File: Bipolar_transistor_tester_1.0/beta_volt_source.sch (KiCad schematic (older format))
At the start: 11 parts, among them IC1 OPA454, Q2 PVG612, U5 CPC1977, U6 CPC1977, U7 CPC1977

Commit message: tester up
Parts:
- added C24, C25: 100n, Capacitor_SMD:C_0805_2012Metric, symbol Device:C
- added R? (x4): 1k 1%, Resistor_SMD:R_0805_2012Metric, symbol Device:R
- U31: renamed from U5; footprint (none) -> OptoDevice:i4-PAC
- U33: renamed from U6; footprint (none) -> OptoDevice:i4-PAC
- U34: renamed from U7; footprint (none) -> OptoDevice:i4-PAC
- renumbered D10 to D7, IC1 to IC3, R14 to R43, R15 to R44, R16 to R45, R17 to R46, R18 to R47, Q2 to U32
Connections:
- net +45V: now also C25.1
- net -45V: now also C24.1
- net GND: now also C24.2, C25.2
- net at IC3.6, U32.6: now also U33.2, U34.2; no longer U33.4, U34.4
- net 6_bvs1: now reaches U31.3
- net at U31.4: now also R?.1
- net to_collector: now reaches U34.1
- net to_base: now reaches U33.1
- net at U32.1: now also R?.1
- net 6_bvs2: now reaches U32.2
- net dac renamed dac1
- net feedback renamed collector_feedback
- net out_base renamed 6_bvs4
- net out_collector renamed 6_bvs3
- new net: R?.1, U34.4
- new net: R?.1, U33.4
- new net 6_com_an: R?.2, R?.2, R?.2, R?.2
- no-connect marks 1 -> 3

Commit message: tester up
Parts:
- removed U33: CPC1977, OptoDevice:i4-PAC, symbol Relay_SolidState:CPC1977
- added U33: PVG612, Package_DIP:DIP-6_W7.62mm, symbol Relay_SolidState:PVG612
- gave numbers to parts that had none: 4
- renumbered R43 to R59, R44 to R60, R45 to R62, R46 to R63, R47 to R64
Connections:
- net 6_bvs4: now also U33.2
- net to_base: now also U33.6
- net at IC3.6, U32.6, U34.2: now also U33.4
- net at R66.1: now also U33.1
- no-connect marks 3 -> 4
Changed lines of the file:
@@
 Sheet 8 11
 Title ""
-Date ""
+Date "2022-04-25"
 Rev ""
 Comp ""
@@
 $EndComp
 $Comp
-L Device:R R45
+L Device:R R62
 U 1 1 626C0321
 P 5125 4200
-F 0 "R45" H 5195 4246 50  0000 L CNN
+F 0 "R62" H 5195 4246 50  0000 L CNN
 F 1 "1M 1%" H 5195 4155 50  0000 L CNN
 F 2 "Resistor_SMD:R_0805_2012Metric" V 5055 4200 50  0001 C CNN
@@
 $EndComp
 $Comp
-L Device:R R44
+L Device:R R60
 U 1 1 626C0D69
 P 4850 3900
-F 0 "R44" V 4643 3900 50  0000 C CNN
+F 0 "R60" V 4643 3900 50  0000 C CNN
 F 1 "200k" V 4734 3900 50  0000 C CNN
 F 2 "Resistor_SMD:R_0805_2012Metric" V 4780 3900 50  0001 C CNN
@@
 $EndComp
 $Comp
-L Device:R R43
+L Device:R R59
 U 1 1 626C163D
 P 4850 3500
-F 0 "R43" V 4643 3500 50  0000 C CNN
+F 0 "R59" V 4643 3500 50  0000 C CNN
 F 1 "200k" V 4734 3500 50  0000 C CNN
 F 2 "Resistor_SMD:R_0805_2012Metric" V 4780 3500 50  0001 C CNN
@@
 $EndComp
 $Comp
-L power:GND #PWR087
+L power:GND #PWR0100
 U 1 1 626C292A
 P 5125 4400
-F 0 "#PWR087" H 5125 4150 50  0001 C CNN
+F 0 "#PWR0100" H 5125 4150 50  0001 C CNN
 F 1 "GND" H 5130 4227 50  0000 C CNN
 F 2 "" H 5125 4400 50  0001 C CNN
@@
 Connection ~ 5125 3900
 $Comp
-L power:GND #PWR086
+L power:GND #PWR099
 U 1 1 626C4849
 P 4500 3500
-F 0 "#PWR086" H 4500 3250 50  0001 C CNN
+F 0 "#PWR099" H 4500 3250 50  0001 C CNN
 F 1 "GND" H 4505 3327 50  0000 C CNN
 F 2 "" H 4500 3500 50  0001 C CNN
@@
 	5450 4275 5450 4200
 $Comp
-L power:-45 #PWR089
+L power:-45 #PWR0102
 U 1 1 626B2C4D
 P 5450 4275
-F 0 "#PWR089" H 5590 4325 50  0001 C CNN
+F 0 "#PWR0102" H 5590 4325 50  0001 C CNN
 F 1 "-45" H 5465 4448 50  0000 C CNN
 F 2 "" H 5450 4275 50  0001 C CNN
@@
 $EndComp
 $Comp
-L power:+45 #PWR088
+L power:+45 #PWR0101
 U 1 1 626B5D57
 P 5450 2825
-F 0 "#PWR088" H 5570 2865 50  0001 C CNN
+F 0 "#PWR0101" H 5570 2865 50  0001 C CNN
 F 1 "+45" H 5465 2998 50  0000 C CNN
 F 2 "" H 5450 2825 50  0001 C CNN
@@
 $EndComp
 $Comp
-L Device:R R46
+L Device:R R63
 U 1 1 626C68FB
 P 5550 2400
-F 0 "R46" V 5343 2400 50  0000 C CNN
+F 0 "R63" V 5343 2400 50  0000 C CNN
 F 1 "1M 1%" V 5434 2400 50  0000 C CNN
 F 2 "Resistor_SMD:R_0805_2012Metric" V 5480 2400 50  0001 C CNN
@@
 Wire Wire Line
 	6350 3700 6550 3700
-$Comp
-L Relay_SolidState:CPC1977 U33
-U 1 1 626F7078
-P 7600 5150
-F 0 "U33" V 7646 4970 50  0000 R CNN
-F 1 "CPC1977" V 7555 4970 50  0000 R CNN
-F 2 "OptoDevice:i4-PAC" H 7600 5200 50  0001 C CNN
-F 3 "" H 7600 5200 50  0001 C CNN
-	1    7600 5150
-	0    1    1    0
-$EndComp
 Text HLabel 8050 4850 2    50   Output ~ 0
 to_base
@@
 	5750 4150 5750 4000
 $Comp
-L power:-45 #PWR091
+L power:-45 #PWR0104
 U 1 1 626FD9F5
 P 5750 4150
-F 0 "#PWR091" H 5890 4200 50  0001 C CNN
+F 0 "#PWR0104" H 5890 4200 50  0001 C CNN
 F 1 "-45" H 5765 4323 50  0000 C CNN
 F 2 "" H 5750 4150 50  0001 C CNN
@@
 	5450 2825 5450 3200
 $Comp
-L Device:R R47
+L Device:R R64
 U 1 1 627039AF
 P 5750 2900
-F 0 "R47" H 5820 2946 50  0000 L CNN
+F 0 "R64" H 5820 2946 50  0000 L CNN
 F 1 "100k" H 5820 2855 50  0000 L CNN
 F 2 "Resistor_SMD:R_0805_2012Metric" V 5680 2900 50  0001 C CNN
@@
 $EndComp
 $Comp
-L power:-45 #PWR092
+L power:-45 #PWR0105
 U 1 1 627066A8
 P 6250 3250
-F 0 "#PWR092" H 6390 3300 50  0001 C CNN
+F 0 "#PWR0105" H 6390 3300 50  0001 C CNN
 F 1 "-45" H 6265 3423 50  0000 C CNN
 F 2 "" H 6250 3250 50  0001 C CNN
@@
 	5900 3250 5750 3250
 $Comp
-L power:+45 #PWR090
+L power:+45 #PWR0103
 U 1 1 6270E004
 P 5750 2700
-F 0 "#PWR090" H 5870 2740 50  0001 C CNN
+F 0 "#PWR0103" H 5870 2740 50  0001 C CNN
 F 1 "+45" H 5765 2873 50  0000 C CNN
 F 2 "" H 5750 2700 50  0001 C CNN
@@
 AR Path="/62558810/62AD2268" Ref="#PWR?"  Part="1"
 AR Path="/62558C62/62AD2268" Ref="#PWR?"  Part="1"
-AR Path="/625CBC7B/62AD2268" Ref="#PWR084"  Part="1"
-F 0 "#PWR084" H 3550 5150 50  0001 C CNN
+AR Path="/625CBC7B/62AD2268" Ref="#PWR097"  Part="1"
+F 0 "#PWR097" H 3550 5150 50  0001 C CNN
 F 1 "GND" H 3555 5227 50  0000 C CNN
 F 2 "" H 3550 5400 50  0001 C CNN
@@
 	3550 5250 3300 5250
 $Comp
-L power:-45 #PWR083
+L power:-45 #PWR096
 U 1 1 62AD32DB
 P 3300 4850
-F 0 "#PWR083" H 3440 4900 50  0001 C CNN
+F 0 "#PWR096" H 3440 4900 50  0001 C CNN
 F 1 "-45" H 3315 5023 50  0000 C CNN
 F 2 "" H 3300 4850 50  0001 C CNN
@@
 $EndComp
 $Comp
-L power:+45 #PWR085
+L power:+45 #PWR098
 U 1 1 62AD3FE9
 P 3750 4850
-F 0 "#PWR085" H 3870 4890 50  0001 C CNN
+F 0 "#PWR098" H 3870 4890 50  0001 C CNN
 F 1 "+45" H 3765 5023 50  0000 C CNN
 F 2 "" H 3750 4850 50  0001 C CNN
@@
 6_com_an
 $Comp
-L Device:R R?
+L Device:R R61
 U 1 1 627FF865
 P 5050 1850
-F 0 "R?" V 5150 1850 50  0000 C CNN
+F 0 "R61" V 5150 1850 50  0000 C CNN
 F 1 "1k 1%" V 5250 1850 50  0000 C CNN
 F 2 "Resistor_SMD:R_0805_2012Metric" V 4980 1850 50  0001 C CNN
@@
 6_com_an
 $Comp
-L Device:R R?
+L Device:R R65
 U 1 1 62801DEE
 P 7450 2950
-F 0 "R?" V 7350 2950 50  0000 C CNN
+F 0 "R65" V 7350 2950 50  0000 C CNN
 F 1 "1k 1%" V 7250 2950 50  0000 C CNN
 F 2 "Resistor_SMD:R_0805_2012Metric" V 7380 2950 50  0001 C CNN
@@
 	7300 2950 7150 2950
 $Comp
-L Device:R R?
+L Device:R R67
 U 1 1 628067B9
 P 7950 4400
-F 0 "R?" V 7850 4400 50  0000 C CNN
+F 0 "R67" V 7850 4400 50  0000 C CNN
 F 1 "1k 1%" V 7750 4400 50  0000 C CNN
 F 2 "Resistor_SMD:R_0805_2012Metric" V 7880 4400 50  0001 C CNN
@@
 	7750 4400 7750 4300
 $Comp
-L Device:R R?
+L Device:R R66
 U 1 1 62809726
 P 7900 5550
-F 0 "R?" V 7800 5550 50  0000 C CNN
+F 0 "R66" V 7800 5550 50  0000 C CNN
 F 1 "1k 1%" V 7700 5550 50  0000 C CNN
 F 2 "Resistor_SMD:R_0805_2012Metric" V 7830 5550 50  0001 C CNN
@@
 Wire Wire Line
 	7500 5550 7500 5450
+$Comp
+L Relay_SolidState:PVG612 U33
+U 1 1 627C7E59
+P 7600 5150
+F 0 "U33" H 7600 4825 50  0000 C CNN
+F 1 "PVG612" H 7600 4916 50  0000 C CNN
+F 2 "Package_DIP:DIP-6_W7.62mm" H 7600 5150 50  0001 L BNN
+F 3 "" H 7600 5150 50  0001 L BNN
+F 4 "International Rectifier" H 7600 5150 50  0001 L BNN "MANUFACTURER"
+	1    7600 5150
+	0    1    -1   0
+$EndComp
+NoConn ~ 7600 4850
 $EndSCHEMATC

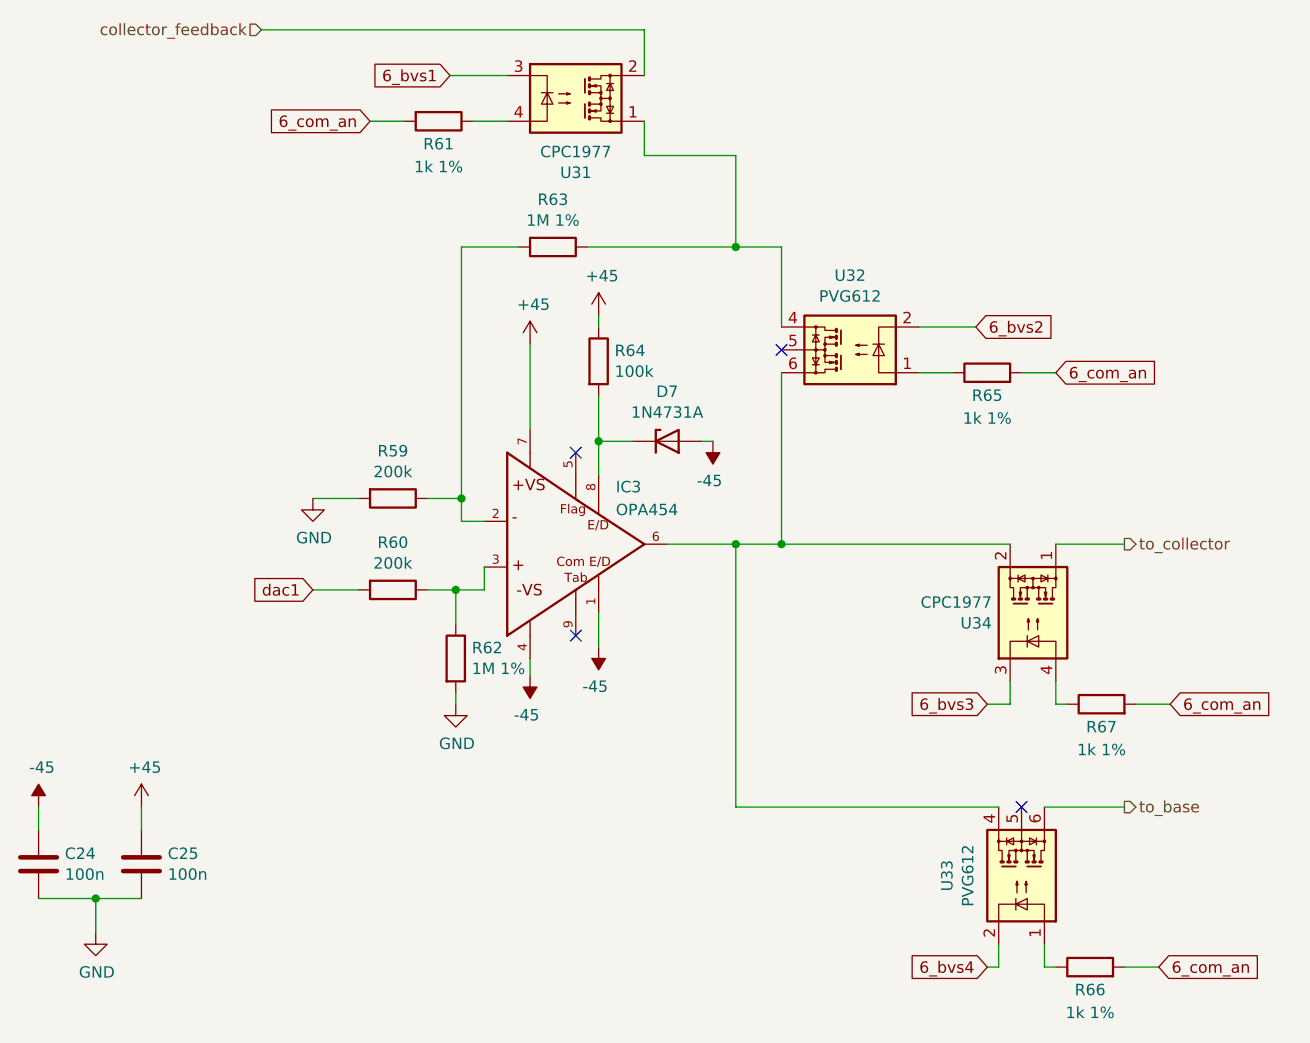
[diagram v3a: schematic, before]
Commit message: edit resistors cpc1977
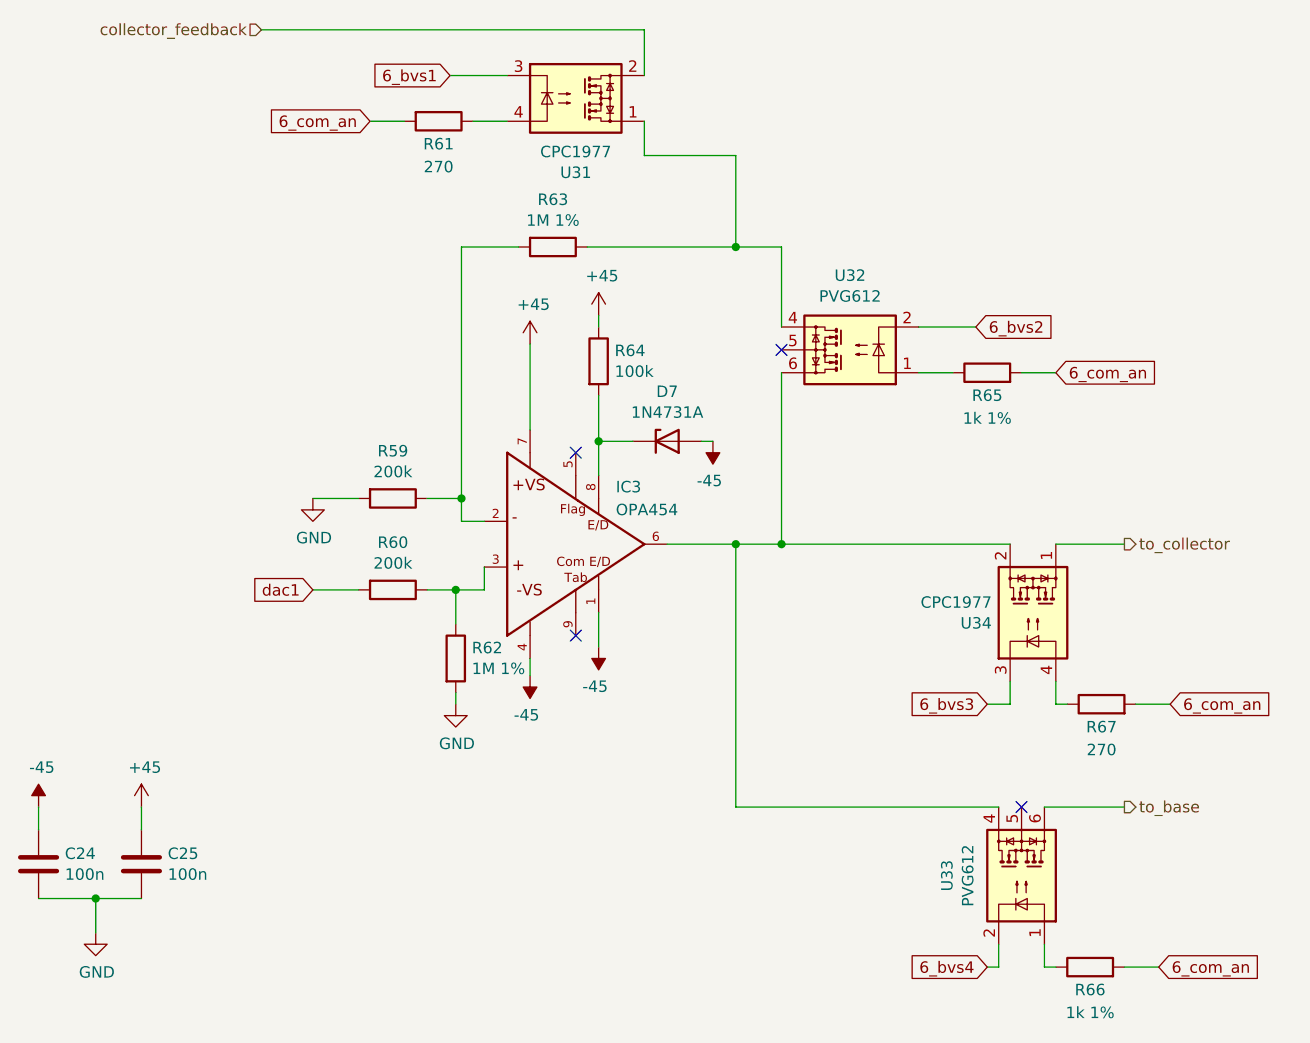
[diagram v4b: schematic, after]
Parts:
- R61, R67: value 1k 1% -> 270
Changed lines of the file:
@@
 P 5050 1850
 F 0 "R61" V 5150 1850 50  0000 C CNN
-F 1 "1k 1%" V 5250 1850 50  0000 C CNN
+F 1 "270" V 5250 1850 50  0000 C CNN
 F 2 "Resistor_SMD:R_0805_2012Metric" V 4980 1850 50  0001 C CNN
 F 3 "~" H 5050 1850 50  0001 C CNN
@@
 P 7950 4400
 F 0 "R67" V 7850 4400 50  0000 C CNN
-F 1 "1k 1%" V 7750 4400 50  0000 C CNN
+F 1 "270" V 7750 4400 50  0000 C CNN
 F 2 "Resistor_SMD:R_0805_2012Metric" V 7880 4400 50  0001 C CNN
 F 3 "~" H 7950 4400 50  0001 C CNN
